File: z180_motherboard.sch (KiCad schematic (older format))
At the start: 7 parts

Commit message: added more chips
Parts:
- removed U? (x6): EPM7064STC100, symbol CPLD_Altera:EPM7064STC100
- added J1, J3: Conn_02x40_Counter_Clockwise, Connector_PinSocket_2.54mm:PinSocket_2x40_P2.54mm_Vertical, symbol Connector_Generic:Conn_02x40_Counter_Clockwise
- added J2: Conn_02x40_Counter_Clockwise, Connector_PinSocket_2.54mm:PinSocket_2x40_P2.54mm_Horizontal, symbol Connector_Generic:Conn_02x40_Counter_Clockwise
- added U1: EPM7064STC200, Package_QFP:TQFP-100-1EP_14x14mm_P0.5mm_EP5x5mm_ThermalVias, symbol CPLD_Altera:EPM7064STC200
- added U3, U4: SST39SF040, Package_LCC:PLCC-32_SMD-Socket, symbol Memory_Flash:SST39SF040
- added U5: AS6C4008-55PCN, Package_SO:TSSOP-32_6.1x11mm_P0.65mm, symbol Memory_RAM:AS6C4008-55PCN
- added U6: DS1302S+, Package_SO:SO-8_5.3x6.2mm_P1.27mm, symbol Timer_RTC:DS1302S+
- gave numbers to parts that had none: 1
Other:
- moved on the sheet: U2
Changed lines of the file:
@@
 $Descr A4 11693 8268
 encoding utf-8
-Sheet 1 1
+Sheet 1 2
 Title ""
 Date ""
@@
 $EndDescr
 $Comp
-L CPU:Z8S18033FSC U?
+L CPU:Z8S18033FSC U2
 U 1 1 5D319D1A
-P 1800 2900
-F 0 "U?" H 1800 4981 50  0000 C CNN
-F 1 "Z8S18033FSC" H 1800 4890 50  0000 C CNN
-F 2 "QFP80P1792X2392X310-80N" H 2700 4600 50  0001 L CNN
-F 3 "https://mouser.componentsearchengine.com/Datasheets/1/Z8S18033FSC.pdf" H 2700 4500 50  0001 L CNN
-F 4 "Microprocessors - MPU 33MHz STATIC Z180" H 2700 4700 50  0001 L CNN "Description"
-F 5 "3.1" H 2700 4600 50  0001 L CNN "Height"
-F 6 "Zilog" H 900 3850 50  0001 L CNN "Manufacturer_Name"
-F 7 "Z8S18033FSC" H 3450 4400 50  0001 L CNN "Manufacturer_Part_Number"
-	1    1800 2900
+P 2200 2800
+F 0 "U2" H 2200 4881 50  0000 C CNN
+F 1 "Z8S18033FSC" H 2200 4790 50  0000 C CNN
+F 2 "QFP80P1792X2392X310-80N" H 3100 4500 50  0001 L CNN
+F 3 "https://mouser.componentsearchengine.com/Datasheets/1/Z8S18033FSC.pdf" H 3100 4400 50  0001 L CNN
+F 4 "Microprocessors - MPU 33MHz STATIC Z180" H 3100 4600 50  0001 L CNN "Description"
+F 5 "3.1" H 3100 4500 50  0001 L CNN "Height"
+F 6 "Zilog" H 1300 3750 50  0001 L CNN "Manufacturer_Name"
+F 7 "Z8S18033FSC" H 3850 4300 50  0001 L CNN "Manufacturer_Part_Number"
+	1    2200 2800
 	1    0    0    -1
 $EndComp
 $Comp
-L CPLD_Altera:EPM7064STC100 U?
-U 1 1 5D31D181
-P 4950 1250
-F 0 "U?" H 5319 661 50  0000 L CNN
-F 1 "EPM7064STC100" H 5319 570 50  0000 L CNN
-F 2 "" H 4050 1650 50  0001 C CNN
-F 3 "" H 4050 1650 50  0001 C CNN
-	1    4950 1250
+L CPLD_Altera:EPM7064STC200 U1
+U 1 1 5D300041
+P 4750 1500
+F 0 "U1" H 4450 2450 50  0000 L CNN
+F 1 "EPM7064STC200" H 4450 2350 50  0000 L CNN
+F 2 "Package_QFP:TQFP-100-1EP_14x14mm_P0.5mm_EP5x5mm_ThermalVias" H 4550 2450 50  0001 C CNN
+F 3 "https://www.intel.com/content/dam/www/programmable/us/en/pdfs/literature/ds/archives/m7000.pdf" H 4550 2450 50  0001 C CNN
+	1    4750 1500
 	1    0    0    -1
 $EndComp
 $Comp
-L CPLD_Altera:EPM7064STC100 U?
-U 2 1 5D322B81
-P 6450 1300
-F 0 "U?" H 6869 711 50  0000 L CNN
-F 1 "EPM7064STC100" H 6869 620 50  0000 L CNN
-F 2 "" H 5550 1700 50  0001 C CNN
-F 3 "" H 5550 1700 50  0001 C CNN
-	2    6450 1300
+L CPLD_Altera:EPM7064STC200 U1
+U 2 1 5D30387B
+P 6150 1500
+F 0 "U1" H 5850 2450 50  0000 L CNN
+F 1 "EPM7064STC200" H 5850 2350 50  0000 L CNN
+F 2 "Package_QFP:TQFP-100-1EP_14x14mm_P0.5mm_EP5x5mm_ThermalVias" H 5950 2450 50  0001 C CNN
+F 3 "https://www.intel.com/content/dam/www/programmable/us/en/pdfs/literature/ds/archives/m7000.pdf" H 5950 2450 50  0001 C CNN
+	2    6150 1500
 	1    0    0    -1
 $EndComp
 $Comp
-L CPLD_Altera:EPM7064STC100 U?
-U 3 1 5D328042
-P 8150 1550
-F 0 "U?" H 8569 1161 50  0000 L CNN
-F 1 "EPM7064STC100" H 8569 1070 50  0000 L CNN
-F 2 "" H 7250 1950 50  0001 C CNN
-F 3 "" H 7250 1950 50  0001 C CNN
-	3    8150 1550
+L CPLD_Altera:EPM7064STC200 U1
+U 3 1 5D30686D
+P 4750 3400
+F 0 "U1" H 4500 4350 50  0000 L CNN
+F 1 "EPM7064STC200" H 4500 4250 50  0000 L CNN
+F 2 "Package_QFP:TQFP-100-1EP_14x14mm_P0.5mm_EP5x5mm_ThermalVias" H 4550 4350 50  0001 C CNN
+F 3 "https://www.intel.com/content/dam/www/programmable/us/en/pdfs/literature/ds/archives/m7000.pdf" H 4550 4350 50  0001 C CNN
+	3    4750 3400
 	1    0    0    -1
 $EndComp
 $Comp
-L CPLD_Altera:EPM7064STC100 U?
-U 4 1 5D32CDF4
-P 4950 3800
-F 0 "U?" H 5369 3661 50  0000 L CNN
-F 1 "EPM7064STC100" H 5369 3570 50  0000 L CNN
-F 2 "" H 4050 4200 50  0001 C CNN
-F 3 "" H 4050 4200 50  0001 C CNN
-	4    4950 3800
+L CPLD_Altera:EPM7064STC200 U1
+U 4 1 5D30BD12
+P 6150 3400
+F 0 "U1" H 5900 4350 50  0000 L CNN
+F 1 "EPM7064STC200" H 5900 4250 50  0000 L CNN
+F 2 "Package_QFP:TQFP-100-1EP_14x14mm_P0.5mm_EP5x5mm_ThermalVias" H 5950 4350 50  0001 C CNN
+F 3 "https://www.intel.com/content/dam/www/programmable/us/en/pdfs/literature/ds/archives/m7000.pdf" H 5950 4350 50  0001 C CNN
+	4    6150 3400
 	1    0    0    -1
 $EndComp
 $Comp
-L CPLD_Altera:EPM7064STC100 U?
-U 5 1 5D33121E
-P 6550 3800
-F 0 "U?" H 7369 3661 50  0000 L CNN
-F 1 "EPM7064STC100" H 7369 3570 50  0000 L CNN
-F 2 "" H 5650 4200 50  0001 C CNN
-F 3 "" H 5650 4200 50  0001 C CNN
-	5    6550 3800
+L CPLD_Altera:EPM7064STC200 U1
+U 5 1 5D30FC95
+P 7500 1500
+F 0 "U1" H 7200 2450 50  0000 L CNN
+F 1 "EPM7064STC200" H 7200 2350 50  0000 L CNN
+F 2 "Package_QFP:TQFP-100-1EP_14x14mm_P0.5mm_EP5x5mm_ThermalVias" H 7300 2450 50  0001 C CNN
+F 3 "https://www.intel.com/content/dam/www/programmable/us/en/pdfs/literature/ds/archives/m7000.pdf" H 7300 2450 50  0001 C CNN
+	5    7500 1500
 	1    0    0    -1
 $EndComp
 $Comp
-L CPLD_Altera:EPM7064STC100 U?
-U 6 1 5D335EF9
-P 8500 3650
-F 0 "U?" H 8869 2268 50  0000 L CNN
-F 1 "EPM7064STC100" H 8869 2177 50  0000 L CNN
-F 2 "" H 7600 4050 50  0001 C CNN
-F 3 "" H 7600 4050 50  0001 C CNN
-	6    8500 3650
+L CPLD_Altera:EPM7064STC200 U1
+U 6 1 5D3158FE
+P 7550 3650
+F 0 "U1" H 7550 4831 50  0000 C CNN
+F 1 "EPM7064STC200" H 7550 4740 50  0000 C CNN
+F 2 "Package_QFP:TQFP-100-1EP_14x14mm_P0.5mm_EP5x5mm_ThermalVias" H 7350 4600 50  0001 C CNN
+F 3 "https://www.intel.com/content/dam/www/programmable/us/en/pdfs/literature/ds/archives/m7000.pdf" H 7350 4600 50  0001 C CNN
+	6    7550 3650
 	1    0    0    -1
 $EndComp
+$Comp
+L Memory_Flash:SST39SF040 U3
+U 1 1 5D338FCA
+P 3250 6400
+F 0 "U3" H 3250 7881 50  0000 C CNN
+F 1 "SST39SF040" H 3250 7790 50  0000 C CNN
+F 2 "Package_LCC:PLCC-32_SMD-Socket" H 3250 6700 50  0001 C CNN
+F 3 "http://ww1.microchip.com/downloads/en/DeviceDoc/25022B.pdf" H 3250 6700 50  0001 C CNN
+	1    3250 6400
+	1    0    0    -1
+$EndComp
+$Comp
+L Memory_Flash:SST39SF040 U4
+U 1 1 5D33A84D
+P 4850 6400
+F 0 "U4" H 4850 7881 50  0000 C CNN
+F 1 "SST39SF040" H 4850 7790 50  0000 C CNN
+F 2 "Package_LCC:PLCC-32_SMD-Socket" H 4850 6700 50  0001 C CNN
+F 3 "http://ww1.microchip.com/downloads/en/DeviceDoc/25022B.pdf" H 4850 6700 50  0001 C CNN
+	1    4850 6400
+	1    0    0    -1
+$EndComp
+$Comp
+L Memory_RAM:AS6C4008-55PCN U5
+U 1 1 5D33C5D8
+P 6200 6500
+F 0 "U5" H 6200 7781 50  0000 C CNN
+F 1 "AS6C4008-55PCN" H 6200 7690 50  0000 C CNN
+F 2 "Package_SO:TSSOP-32_6.1x11mm_P0.65mm" H 6200 6600 50  0001 C CNN
+F 3 "https://www.alliancememory.com/wp-content/uploads/pdf/AS6C4008.pdf" H 6200 6600 50  0001 C CNN
+	1    6200 6500
+	1    0    0    -1
+$EndComp
+$Comp
+L Connector_Generic:Conn_02x40_Counter_Clockwise J1
+U 1 1 5D352A6A
+P 8684 3147
+F 0 "J1" H 8734 5264 50  0000 C CNN
+F 1 "Conn_02x40_Counter_Clockwise" H 8734 5173 50  0000 C CNN
+F 2 "Connector_PinSocket_2.54mm:PinSocket_2x40_P2.54mm_Vertical" H 8684 3147 50  0001 C CNN
+F 3 "~" H 8684 3147 50  0001 C CNN
+	1    8684 3147
+	1    0    0    -1
+$EndComp
+$Comp
+L Connector_Generic:Conn_02x40_Counter_Clockwise J3
+U 1 1 5D35A9F1
+P 9650 3150
+F 0 "J3" H 9700 5267 50  0000 C CNN
+F 1 "Conn_02x40_Counter_Clockwise" H 9700 5176 50  0000 C CNN
+F 2 "Connector_PinSocket_2.54mm:PinSocket_2x40_P2.54mm_Vertical" H 9650 3150 50  0001 C CNN
+F 3 "~" H 9650 3150 50  0001 C CNN
+	1    9650 3150
+	1    0    0    -1
+$EndComp
+$Comp
+L Connector_Generic:Conn_02x40_Counter_Clockwise J2
+U 1 1 5D38AC9D
+P 10650 3100
+F 0 "J2" H 10700 5217 50  0000 C CNN
+F 1 "Conn_02x40_Counter_Clockwise" H 10700 5126 50  0000 C CNN
+F 2 "Connector_PinSocket_2.54mm:PinSocket_2x40_P2.54mm_Horizontal" H 10650 3100 50  0001 C CNN
+F 3 "~" H 10650 3100 50  0001 C CNN
+	1    10650 3100
+	1    0    0    -1
+$EndComp
+$Comp
+L Timer_RTC:DS1302S+ U6
+U 1 1 5D3BF133
+P 8050 5950
+F 0 "U6" H 8594 5996 50  0000 L CNN
+F 1 "DS1302S+" H 8594 5905 50  0000 L CNN
+F 2 "Package_SO:SO-8_5.3x6.2mm_P1.27mm" H 8050 5450 50  0001 C CNN
+F 3 "https://datasheets.maximintegrated.com/en/ds/DS1302.pdf" H 7600 6350 50  0001 C CNN
+	1    8050 5950
+	1    0    0    -1
+$EndComp
+$Sheet
+S 650  6150 1550 1150
+U 5D3BF5C9
+F0 "Sheet5D3BF5C8" 50
+F1 "clocks.sch" 50
+$EndSheet
 $EndSCHEMATC

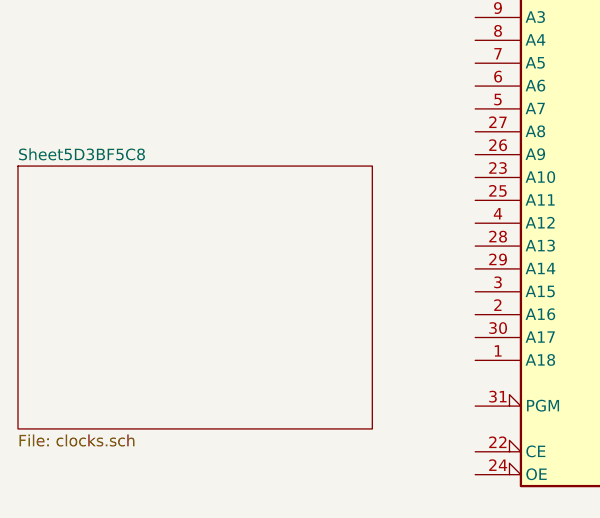
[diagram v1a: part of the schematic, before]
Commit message: removed rescue and cache from .gitignore
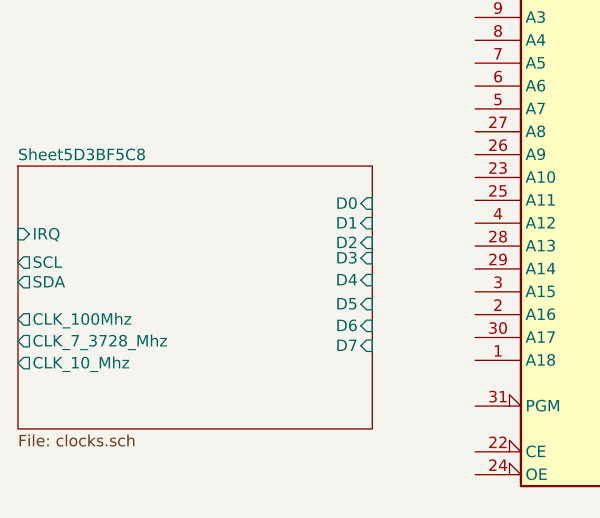
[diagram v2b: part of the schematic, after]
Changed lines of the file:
@@
 F0 "Sheet5D3BF5C8" 50
 F1 "clocks.sch" 50
+F2 "D0" I R 2200 6314 50
+F3 "D1" I R 2200 6400 50
+F4 "D2" I R 2200 6486 50
+F5 "D3" I R 2200 6553 50
+F6 "D4" I R 2200 6649 50
+F7 "D5" I R 2200 6754 50
+F8 "D6" I R 2200 6849 50
+F9 "D7" I R 2200 6936 50
+F10 "IRQ" I L 650 6448 50
+F11 "SCL" O L 650 6572 50
+F12 "SDA" O L 650 6658 50
+F13 "CLK_100Mhz" O L 650 6821 50
+F14 "CLK_7_3728_Mhz" O L 650 6916 50
+F15 "CLK_10_Mhz" O L 650 7012 50
 $EndSheet
 $EndSCHEMATC
